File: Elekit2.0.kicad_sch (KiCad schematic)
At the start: 26 parts, among them J1 USB_C_Receptacle_USB2.0, Q1 AO3401A, SW1 SW_Push, SW2 SW_Push, U1 ESP32-C3-WROOM-02-H4, U2 XC6206P332MR, U3 SRV05-4-P-T7

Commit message: Added ESD protection for USB-C connector
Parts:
- added C?: 4.7n, Capacitor_SMD:C_0402_1005Metric, symbol Device:C_Small
- added R?: 1M, Resistor_SMD:R_1206_3216Metric, symbol Device:R
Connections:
- net GND: now also C?.2, R?.2; no longer J1.S1 (SHIELD)
- new net SHIELD_USB: C?.1, J1.S1 (SHIELD), R?.1
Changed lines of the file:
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@@
   (junction (at 78.74 59.69) (diameter 0) (color 0 0 0 0)
   )
+  (junction (at 26.67 93.98) (diameter 0) (color 0 0 0 0)
+  )
   (junction (at 73.66 68.58) (diameter 0) (color 0 0 0 0)
   )
@@
   )
   (junction (at 49.53 59.69) (diameter 0) (color 0 0 0 0)
+  )
+  (junction (at 26.67 104.14) (diameter 0) (color 0 0 0 0)
   )
   (junction (at 241.935 146.685) (diameter 0) (color 0 0 0 0)
@@
     (stroke (width 0) (type default) (color 0 0 0 0))
   )
+  (wire (pts (xy 22.86 101.6) (xy 22.86 104.14))
+    (stroke (width 0) (type default) (color 0 0 0 0))
+  )
   (wire (pts (xy 193.04 85.09) (xy 194.31 85.09))
     (stroke (width 0) (type default) (color 0 0 0 0))
   )
+  (wire (pts (xy 22.86 96.52) (xy 22.86 93.98))
+    (stroke (width 0) (type default) (color 0 0 0 0))
+  )
   (wire (pts (xy 203.2 105.41) (xy 203.2 104.14))
     (stroke (width 0) (type default) (color 0 0 0 0))
@@
     (stroke (width 0) (type default) (color 0 0 0 0))
   )
+  (wire (pts (xy 26.67 93.98) (xy 26.67 95.25))
+    (stroke (width 0) (type default) (color 0 0 0 0))
+  )
   (wire (pts (xy 190.5 31.75) (xy 194.31 31.75))
     (stroke (width 0) (type default) (color 0 0 0 0))
@@
     (stroke (width 0) (type default) (color 0 0 0 0))
   )
+  (wire (pts (xy 26.67 102.87) (xy 26.67 104.14))
+    (stroke (width 0) (type default) (color 0 0 0 0))
+  )
   (wire (pts (xy 48.26 111.76) (xy 48.26 115.57))
     (stroke (width 0) (type default) (color 0 0 0 0))
@@
     (stroke (width 0) (type default) (color 0 0 0 0))
   )
+  (wire (pts (xy 26.67 80.01) (xy 26.67 93.98))
+    (stroke (width 0) (type default) (color 0 0 0 0))
+  )
   (wire (pts (xy 140.97 34.29) (xy 151.13 34.29))
     (stroke (width 0) (type default) (color 0 0 0 0))
   )
+  (wire (pts (xy 22.86 104.14) (xy 26.67 104.14))
+    (stroke (width 0) (type default) (color 0 0 0 0))
+  )
   (wire (pts (xy 264.16 122.555) (xy 258.445 122.555))
     (stroke (width 0) (type default) (color 0 0 0 0))
@@
     (stroke (width 0) (type default) (color 0 0 0 0))
   )
+  (wire (pts (xy 22.86 93.98) (xy 26.67 93.98))
+    (stroke (width 0) (type default) (color 0 0 0 0))
+  )
   (wire (pts (xy 233.68 146.685) (xy 241.935 146.685))
     (stroke (width 0) (type default) (color 0 0 0 0))
@@
   )
   (wire (pts (xy 186.69 93.98) (xy 186.69 95.25))
+    (stroke (width 0) (type default) (color 0 0 0 0))
+  )
+  (wire (pts (xy 26.67 104.14) (xy 26.67 105.41))
     (stroke (width 0) (type default) (color 0 0 0 0))
   )
@@
   )
   (text "Castor logo" (at 76.2 97.155 0)
+    (effects (font (size 1.27 1.27)) (justify left bottom))
+  )
+  (label "SHIELD_USB" (at 26.67 92.71 90)
     (effects (font (size 1.27 1.27)) (justify left bottom))
   )
@@
     (pin "2")
   )
-  (symbol (lib_id "power:GND") (at 26.67 80.01 0) (unit 1)
-    (in_bom yes) (on_board yes) (fields_autoplaced)
-    (property "Reference" "#PWR0114" (id 0) (at 26.67 86.36 0)
-      (effects (font (size 1.27 1.27)) hide)
-    )
-    (property "Value" "GND" (id 1) (at 26.67 85.09 0))
-    (property "Footprint" "" (id 2) (at 26.67 80.01 0)
-      (effects (font (size 1.27 1.27)) hide)
-    )
-    (property "Datasheet" "" (id 3) (at 26.67 80.01 0)
-      (effects (font (size 1.27 1.27)) hide)
-    )
-    (pin "1")
+  (symbol (lib_id "power:GND") (at 26.67 105.41 0) (unit 1)
+    (in_bom yes) (on_board yes) (fields_autoplaced)
+    (property "Reference" "#PWR0114" (id 0) (at 26.67 111.76 0)
+      (effects (font (size 1.27 1.27)) hide)
+    )
+    (property "Value" "GND" (id 1) (at 26.67 110.49 0))
+    (property "Footprint" "" (id 2) (at 26.67 105.41 0)
+      (effects (font (size 1.27 1.27)) hide)
+    )
+    (property "Datasheet" "" (id 3) (at 26.67 105.41 0)
+      (effects (font (size 1.27 1.27)) hide)
+    )
+    (pin "1")
+  )
+  (symbol (lib_id "Device:C_Small") (at 22.86 99.06 0) (unit 1)
+    (in_bom yes) (on_board yes)
+    (property "Reference" "C?" (id 0) (at 17.78 97.79 0)
+      (effects (font (size 1.27 1.27)) (justify left))
+    )
+    (property "Value" "4.7n" (id 1) (at 16.51 100.33 0)
+      (effects (font (size 1.27 1.27)) (justify left))
+    )
+    (property "Footprint" "Capacitor_SMD:C_0402_1005Metric" (id 2) (at 22.86 99.06 0)
+      (effects (font (size 1.27 1.27)) hide)
+    )
+    (property "Datasheet" "~" (id 3) (at 22.86 99.06 0)
+      (effects (font (size 1.27 1.27)) hide)
+    )
+    (property "LCSC Part #" "C84705" (id 4) (at 22.86 99.06 0)
+      (effects (font (size 1.27 1.27)) hide)
+    )
+    (pin "1")
+    (pin "2")
   )
   (symbol (lib_id "Device:LED") (at 131.445 163.83 90) (unit 1)
@@
     )
     (pin "1")
+  )
+  (symbol (lib_id "Device:R") (at 26.67 99.06 0) (unit 1)
+    (in_bom yes) (on_board yes)
+    (property "Reference" "R?" (id 0) (at 29.21 96.52 90))
+    (property "Value" "1M" (id 1) (at 29.21 100.33 90))
+    (property "Footprint" "Resistor_SMD:R_1206_3216Metric" (id 2) (at 24.892 99.06 90)
+      (effects (font (size 1.27 1.27)) hide)
+    )
+    (property "Datasheet" "~" (id 3) (at 26.67 99.06 0)
+      (effects (font (size 1.27 1.27)) hide)
+    )
+    (property "LCSC Part #" "C17927" (id 4) (at 26.67 99.06 0)
+      (effects (font (size 1.27 1.27)) hide)
+    )
+    (pin "1")
+    (pin "2")
   )
   (symbol (lib_id "power:+3.3V") (at 156.21 34.29 0) (unit 1)
@@
       (reference "C8") (unit 1) (value "0.1u") (footprint "Capacitor_SMD:C_0402_1005Metric")
     )
+    (path "/21f0e695-365a-43fd-b4a0-9f396487544d"
+      (reference "C?") (unit 1) (value "4.7n") (footprint "Capacitor_SMD:C_0402_1005Metric")
+    )
     (path "/2f10adcb-9e44-4857-a672-9774ac404abb"
       (reference "D1") (unit 1) (value "1N5819WS") (footprint "Diode_SMD:D_SOD-323")
@@
       (reference "R5") (unit 1) (value "10k") (footprint "Resistor_SMD:R_1206_3216Metric")
     )
+    (path "/6a67c306-4a9e-4e7d-b7ee-094b84b5ac7f"
+      (reference "R?") (unit 1) (value "1M") (footprint "Resistor_SMD:R_1206_3216Metric")
+    )
     (path "/6f7c7881-5fe1-44a3-9b85-9baf12a50d48"

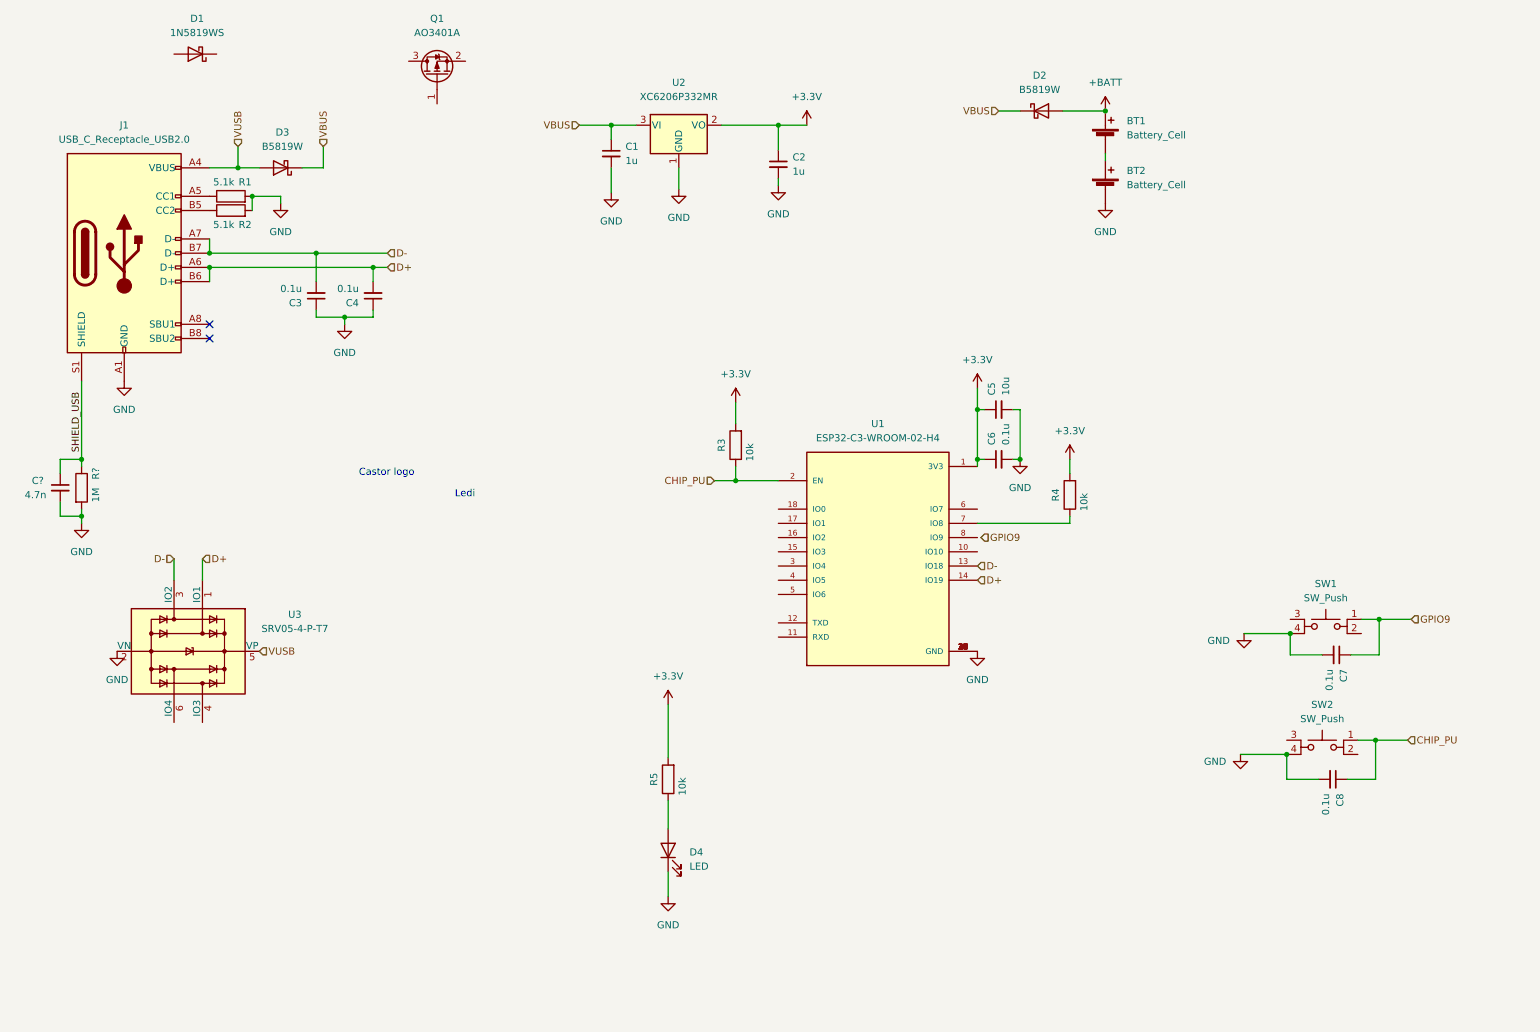
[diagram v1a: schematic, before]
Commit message: Add libraries for used JLCPCB parts. Replace used parts with JLCPCB parts. Start adding LCD support using a shift register
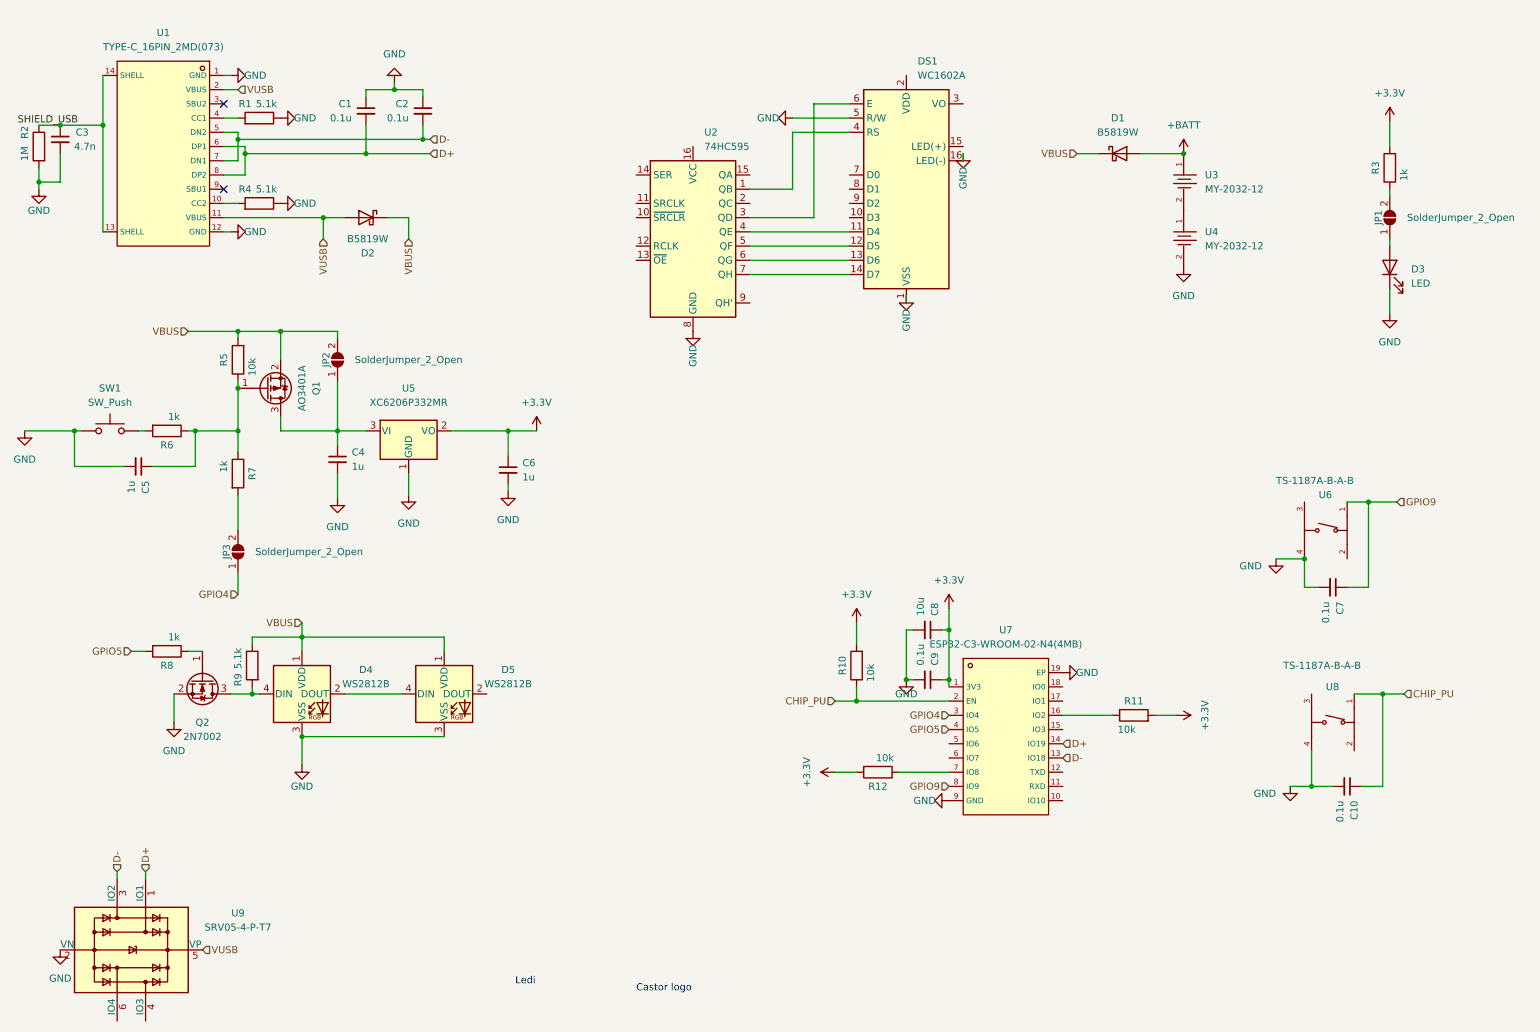
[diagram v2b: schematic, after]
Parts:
- removed BT1, BT2: Battery_Cell, Footprint Libaries:BAT-SMD_MY-2032-12, symbol Device:Battery_Cell
- removed C4, C6: 0.1u, Capacitor_SMD:C_0402_1005Metric, symbol Device:C_Small
- removed C?: 4.7n, Capacitor_SMD:C_0402_1005Metric, symbol Device:C_Small
- removed D1: 1N5819WS, Diode_SMD:D_SOD-323, symbol Diode:1N5819WS
- removed D3: B5819W, Diode_SMD:D_SOD-123, symbol Diode:1N5820
- removed J1: USB_C_Receptacle_USB2.0, Footprint Libaries:USB-C-SMD_TYPE-C-6PIN-2MD-073, symbol Connector:USB_C_Receptacle_USB2.0
- removed R?: 1M, Resistor_SMD:R_1206_3216Metric, symbol Device:R
- removed SW2: SW_Push, Footprint Libaries:SW-SMD_4P-L5.1-W5.1-P3.70-LS6.5-TL-2, symbol Switch:SW_Push
- removed U1: ESP32-C3-WROOM-02-H4, MODULE_ESP32-C3-WROOM-02-H4, symbol Elekit2:ESP32-C3-WROOM-02-H4
- added C1, C2, C9: 0.1u, Capacitor_SMD:C_0805_2012Metric, symbol Device:C_Small
- added C8: 10u, Capacitor_SMD:C_0805_2012Metric, symbol Device:C_Small
- added D2: B5819W, Diode_SMD:D_SOD-123, symbol Diode:1N5820
- added D4, D5: WS2812B, LED_SMD:LED_WS2812B_PLCC4_5.0x5.0mm_P3.2mm, symbol LED:WS2812B
- added DS1: WC1602A, Display:WC1602A, symbol Display_Character:WC1602A
- added JP1, JP2, JP3: SolderJumper_2_Open, Jumper:SolderJumper-2_P1.3mm_Open_RoundedPad1.0x1.5mm, symbol Jumper:SolderJumper_2_Open
- added Q2: 2N7002, Package_TO_SOT_SMD:SOT-23, symbol Transistor_FET:2N7002
- added R10, R11, R12: 10k, Resistor_SMD:R_1206_3216Metric, symbol Device:R
- added R6, R7, R8: 1k, Resistor_SMD:R_0805_2012Metric, symbol Device:R
- added R9: 5.1k, Resistor_SMD:R_0805_2012Metric, symbol Device:R
- added U1: TYPE-C_16PIN_2MD(073), 0_JLCPCB_Footprints:USB-C-SMD_TYPE-C-6PIN-2MD-073, symbol 0_JLCPCB_Symbols:TYPE-C_16PIN_2MD(073)
- added U2: 74HC595, 0_JLCPCB_Footprints:SOIC-16_L9.9-W3.9-P1.27-LS6.0-BL, symbol 74xx:74HC595
- added U3, U4: MY-2032-12, 0_JLCPCB_Footprints:BAT-SMD_MY-2032-12, symbol 0_JLCPCB_Symbols:MY-2032-12
- added U6, U8: TS-1187A-B-A-B, 0_JLCPCB_Footprints:SW-SMD_4P-L5.1-W5.1-P3.70-LS6.5-TL-2, symbol 0_JLCPCB_Symbols:TS-1187A-B-A-B
- added U7: ESP32-C3-WROOM-02-N4(4MB), 0_JLCPCB_Footprints:BULETM-SMD_ESPRESSIF_ESP32-C3-WROOM-02-N4-4MB, symbol 0_JLCPCB_Symbols:ESP32-C3-WROOM-02-N4(4MB)
- C10: renamed from C8; footprint Capacitor_SMD:C_0402_1005Metric -> Capacitor_SMD:C_0805_2012Metric; LCSC (none) -> C28233; LCSC Part # C307331 -> (none)
- C3: value 0.1u -> 4.7n; footprint Capacitor_SMD:C_0402_1005Metric -> Capacitor_SMD:C_0805_2012Metric; LCSC (none) -> C1779; LCSC Part # C307331 -> (none)
- C4: renamed from C1; LCSC (none) -> C28323; LCSC Part # C28323 -> (none)
- C5: value 10u -> 1u; footprint Capacitor_SMD:C_0402_1005Metric -> Capacitor_SMD:C_0805_2012Metric; LCSC (none) -> C28323; LCSC Part # C307331 -> (none)
- C6: renamed from C2; LCSC (none) -> C28323; LCSC Part # C28323 -> (none)
- C7: footprint Capacitor_SMD:C_0402_1005Metric -> Capacitor_SMD:C_0805_2012Metric; LCSC (none) -> C28233; LCSC Part # C307331 -> (none)
- D1: renamed from D2; LCSC (none) -> C8598; LCSC Part # C8598 -> (none)
- D3: renamed from D4; footprint (none) -> LED_SMD:LED_0805_2012Metric; LCSC (none) -> C84256
- Q1: LCSC (none) -> C15127; LCSC Part # C15127 -> (none)
- R1: footprint Resistor_SMD:R_1206_3216Metric -> Resistor_SMD:R_0805_2012Metric; LCSC (none) -> C27834; LCSC Part # C4410 -> (none)
- R2: value 5.1k -> 1M; LCSC (none) -> C17927; LCSC Part # C4410 -> (none)
- R3: value 10k -> 1k; footprint Resistor_SMD:R_1206_3216Metric -> Resistor_SMD:R_0805_2012Metric; LCSC (none) -> C17513; LCSC Part # C4410 -> (none)
- R4: value 10k -> 5.1k; footprint Resistor_SMD:R_1206_3216Metric -> Resistor_SMD:R_0805_2012Metric; LCSC (none) -> C27834; LCSC Part # C4410 -> (none)
- R5: LCSC (none) -> C4410; LCSC Part # C4410 -> (none)
- SW1: footprint Footprint Libaries:SW-SMD_4P-L5.1-W5.1-P3.70-LS6.5-TL-2 -> Button_Switch_THT:SW_PUSH_6mm; now left out of the parts list
- U5: renamed from U2; LCSC (none) -> C5446
- U9: renamed from U3; LCSC (none) -> C85364
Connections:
- net +3.3V: now also C8.1, C9.1, R10.2, R11.2, R12.2, U7.1 (3V3); no longer C5.1, R4.2, R5.2
- net +BATT: now also U3.1
- net CHIP_PU: now also R10.1, U7.2 (EN), U8.1 (A); no longer R3.1
- net D+: now also C1.2, U1.6 (DP1), U1.8 (DP2), U7.14 (IO19)
- net D-: now also C2.2, U1.5 (DN2), U1.7 (DN1), U7.13 (IO18); no longer C3.2
- net GND: now also C3.2, R1.1, R4.1, SW1.1, C1.1, C2.1, C8.2, C9.2, D4.3 (VSS), D5.3 (VSS), DS1.1 (VSS), DS1.16 (LED(-)), DS1.5 (R/W), Q2.2 (S), U1.1 (GND), U1.12 (GND), U2.8 (GND), U4.2, U6.4 (D), U7.19 (EP), U7.9 (GND), U8.4 (D); no longer C3.1, R1.2, SW1.4
- net GPIO9: now also U6.1 (A), U7.8 (IO9); no longer SW1.1
- net VBUS: now also Q1.2 (S), R5.2, D2.1 (K), D4.1 (VDD), D5.1 (VDD), JP2.2 (B), R9.1; no longer C4.1, U5.3 (VI)
- net VUSB: now also D2.2 (A), U1.11 (VBUS), U1.2 (VBUS)
- net at D3.2 (A): now also JP1.1 (A); no longer R5.1
- net at R2.1: now also C3.1, U1.13 (SHELL), U1.14 (SHELL)
- net at SW1.2: now also R6.2
- net at Q1.1 (G): now also C5.1, R5.1, R6.1, R7.1
- net at Q1.3 (D): now also C4.1, U5.3 (VI), JP2.1 (A)
- new net: R1.2, U1.4 (CC1)
- new net: R11.1, U7.16 (IO2)
- new net: R12.1, U7.7 (IO8)
- new net: D4.4 (DIN), Q2.3 (D), R9.2
- new net: D4.2 (DOUT), D5.4 (DIN)
- new net: Q2.1 (G), R8.1
- new net: JP3.2 (B), R7.2
- new net: R4.2, U1.10 (CC2)
- new net: DS1.11 (D4), U2.4 (QE)
- new net: DS1.12 (D5), U2.5 (QF)
- new net: DS1.13 (D6), U2.6 (QG)
- new net: DS1.14 (D7), U2.7 (QH)
- new net: DS1.4 (RS), U2.1 (QB)
- new net: DS1.6 (E), U2.3 (QD)
- new net: U3.2, U4.1
- new net: JP1.2 (B), R3.1
- new net GPIO4: JP3.1 (A), U7.3 (IO4)
- new net GPIO5: R8.2, U7.4 (IO5)
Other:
- moved on the sheet: C10, C4, C6, D1, D3, Q1, U5, U9
